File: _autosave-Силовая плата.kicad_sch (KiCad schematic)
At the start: 9 parts, among them Q1 BSP89, Q2 BSP89, Q3 BSP89, Q4 BSP89, Q5 BSP89, Q6 BSP89, U1 HIP2100_SOIC, U2 HIP2100_SOIC, U3 HIP2100_SOIC

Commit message: Вариант с транзисторами в линию
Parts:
- added J1, J2, J3: Conn_01x01, symbol Connector_Generic:Conn_01x01
- U1, U2, U3: footprint Package_DFN_QFN:DFN-8-1EP_3x3mm_P0.5mm_EP1.65x2.38mm -> Package_SO:SOIC-8_3.9x4.9mm_P1.27mm
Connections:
- net A: now also J1.1 (Pin_1)
- net B: now also J2.1 (Pin_1)
- net C: now also J3.1 (Pin_1)
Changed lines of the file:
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@@
+    )
+  )
+  (global_label "B" (shape input) (at 210.82 63.5 270) (fields_autoplaced)
+    (effects (font (size 1.27 1.27)) (justify right))
+    (property "Intersheetrefs" "${INTERSHEET_REFS}" (at 210.82 67.7552 90)
+      (effects (font (size 1.27 1.27)) (justify right) hide)
+    )
+  )
+  (global_label "C" (shape input) (at 220.98 63.5 270) (fields_autoplaced)
+    (effects (font (size 1.27 1.27)) (justify right))
+    (property "Intersheetrefs" "${INTERSHEET_REFS}" (at 220.98 67.7552 90)
+      (effects (font (size 1.27 1.27)) (justify right) hide)
     )
   )
@@
     )
   )
+  (global_label "A" (shape input) (at 200.66 63.5 270) (fields_autoplaced)
+    (effects (font (size 1.27 1.27)) (justify right))
+    (property "Intersheetrefs" "${INTERSHEET_REFS}" (at 200.66 67.5738 90)
+      (effects (font (size 1.27 1.27)) (justify right) hide)
+    )
+  )
   (global_label "G5" (shape input) (at 163.83 66.04 180) (fields_autoplaced)
     (effects (font (size 1.27 1.27)) (justify right))
@@
     )
   )
+  (symbol (lib_id "Connector_Generic:Conn_01x01") (at 220.98 58.42 90) (unit 1)
+    (in_bom yes) (on_board yes) (dnp no) (fields_autoplaced)
+    (property "Reference" "J3" (at 223.52 57.15 90)
+      (effects (font (size 1.27 1.27)) (justify right))
+    )
+    (property "Value" "Conn_01x01" (at 223.52 59.69 90)
+      (effects (font (size 1.27 1.27)) (justify right) hide)
+    )
+    (property "Footprint" "" (at 220.98 58.42 0)
+      (effects (font (size 1.27 1.27)) hide)
+    )
+    (property "Datasheet" "~" (at 220.98 58.42 0)
+      (effects (font (size 1.27 1.27)) hide)
+    )
+    (pin "1")
+    (instances
+      (project "Силовая плата"
+        (path "/96c6fc92-8ec6-44f7-b0dc-9ad8f1acea09"
+          (reference "J3") (unit 1)
+        )
+      )
+    )
+  )
   (symbol (lib_id "power:+12V") (at 130.81 58.42 0) (unit 1)
     (in_bom yes) (on_board yes) (dnp no) (fields_autoplaced)
@@
     )
   )
+  (symbol (lib_id "Connector_Generic:Conn_01x01") (at 210.82 58.42 90) (unit 1)
+    (in_bom yes) (on_board yes) (dnp no) (fields_autoplaced)
+    (property "Reference" "J2" (at 213.36 57.15 90)
+      (effects (font (size 1.27 1.27)) (justify right))
+    )
+    (property "Value" "Conn_01x01" (at 213.36 59.69 90)
+      (effects (font (size 1.27 1.27)) (justify right) hide)
+    )
+    (property "Footprint" "" (at 210.82 58.42 0)
+      (effects (font (size 1.27 1.27)) hide)
+    )
+    (property "Datasheet" "~" (at 210.82 58.42 0)
+      (effects (font (size 1.27 1.27)) hide)
+    )
+    (pin "1")
+    (instances
+      (project "Силовая плата"
+        (path "/96c6fc92-8ec6-44f7-b0dc-9ad8f1acea09"
+          (reference "J2") (unit 1)
+        )
+      )
+    )
+  )
+  (symbol (lib_id "Connector_Generic:Conn_01x01") (at 200.66 58.42 90) (unit 1)
+    (in_bom yes) (on_board yes) (dnp no) (fields_autoplaced)
+    (property "Reference" "J1" (at 203.2 57.15 90)
+      (effects (font (size 1.27 1.27)) (justify right))
+    )
+    (property "Value" "Conn_01x01" (at 203.2 59.69 90)
+      (effects (font (size 1.27 1.27)) (justify right) hide)
+    )
+    (property "Footprint" "" (at 200.66 58.42 0)
+      (effects (font (size 1.27 1.27)) hide)
+    )
+    (property "Datasheet" "~" (at 200.66 58.42 0)
+      (effects (font (size 1.27 1.27)) hide)
+    )
+    (pin "1")
+    (instances
+      (project "Силовая плата"
+        (path "/96c6fc92-8ec6-44f7-b0dc-9ad8f1acea09"
+          (reference "J1") (unit 1)
+        )
+      )
+    )
+  )
   (symbol (lib_id "Driver_FET:HIP2100_SOIC") (at 175.26 113.03 0) (unit 1)
     (in_bom yes) (on_board yes) (dnp no) (fields_autoplaced)
@@
       (effects (font (size 1.27 1.27)))
     )
-    (property "Footprint" "Package_DFN_QFN:DFN-8-1EP_3x3mm_P0.5mm_EP1.65x2.38mm" (at 175.26 125.73 0)
+    (property "Footprint" "Package_SO:SOIC-8_3.9x4.9mm_P1.27mm" (at 175.26 125.73 0)
       (effects (font (size 1.27 1.27) italic) hide)
     )
@@
       (effects (font (size 1.27 1.27)))
     )
-    (property "Footprint" "Package_DFN_QFN:DFN-8-1EP_3x3mm_P0.5mm_EP1.65x2.38mm" (at 154.94 125.73 0)
+    (property "Footprint" "Package_SO:SOIC-8_3.9x4.9mm_P1.27mm" (at 154.94 125.73 0)
       (effects (font (size 1.27 1.27) italic) hide)
     )
@@
       (effects (font (size 1.27 1.27)))
     )
-    (property "Footprint" "Package_DFN_QFN:DFN-8-1EP_3x3mm_P0.5mm_EP1.65x2.38mm" (at 104.14 86.36 0)
+    (property "Footprint" "Package_SO:SOIC-8_3.9x4.9mm_P1.27mm" (at 104.14 86.36 0)
       (effects (font (size 1.27 1.27) italic) hide)
     )

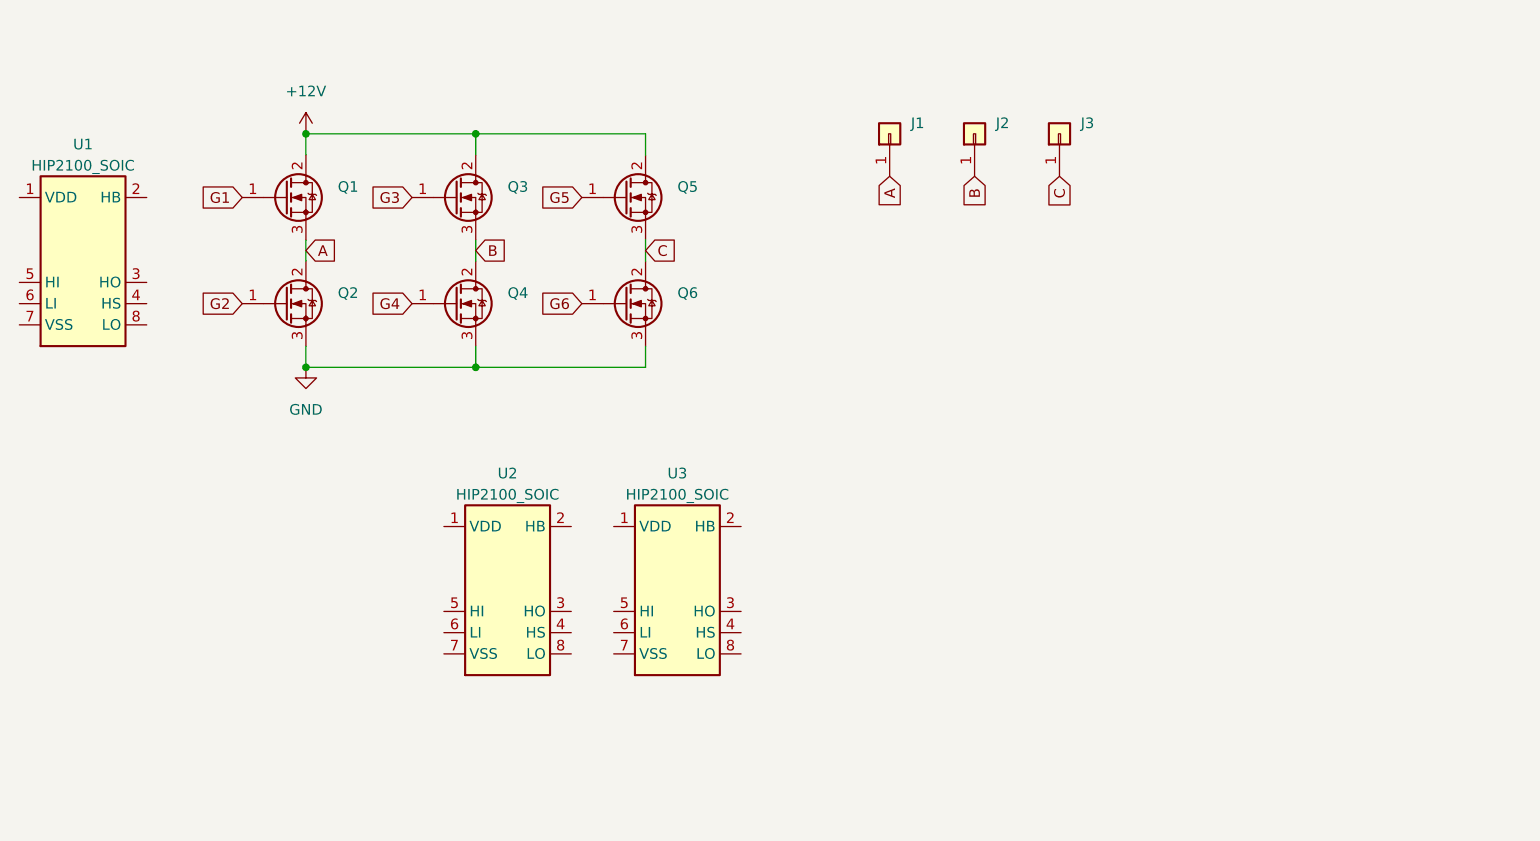
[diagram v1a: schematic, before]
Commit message: Добавил датчики тока и шунты
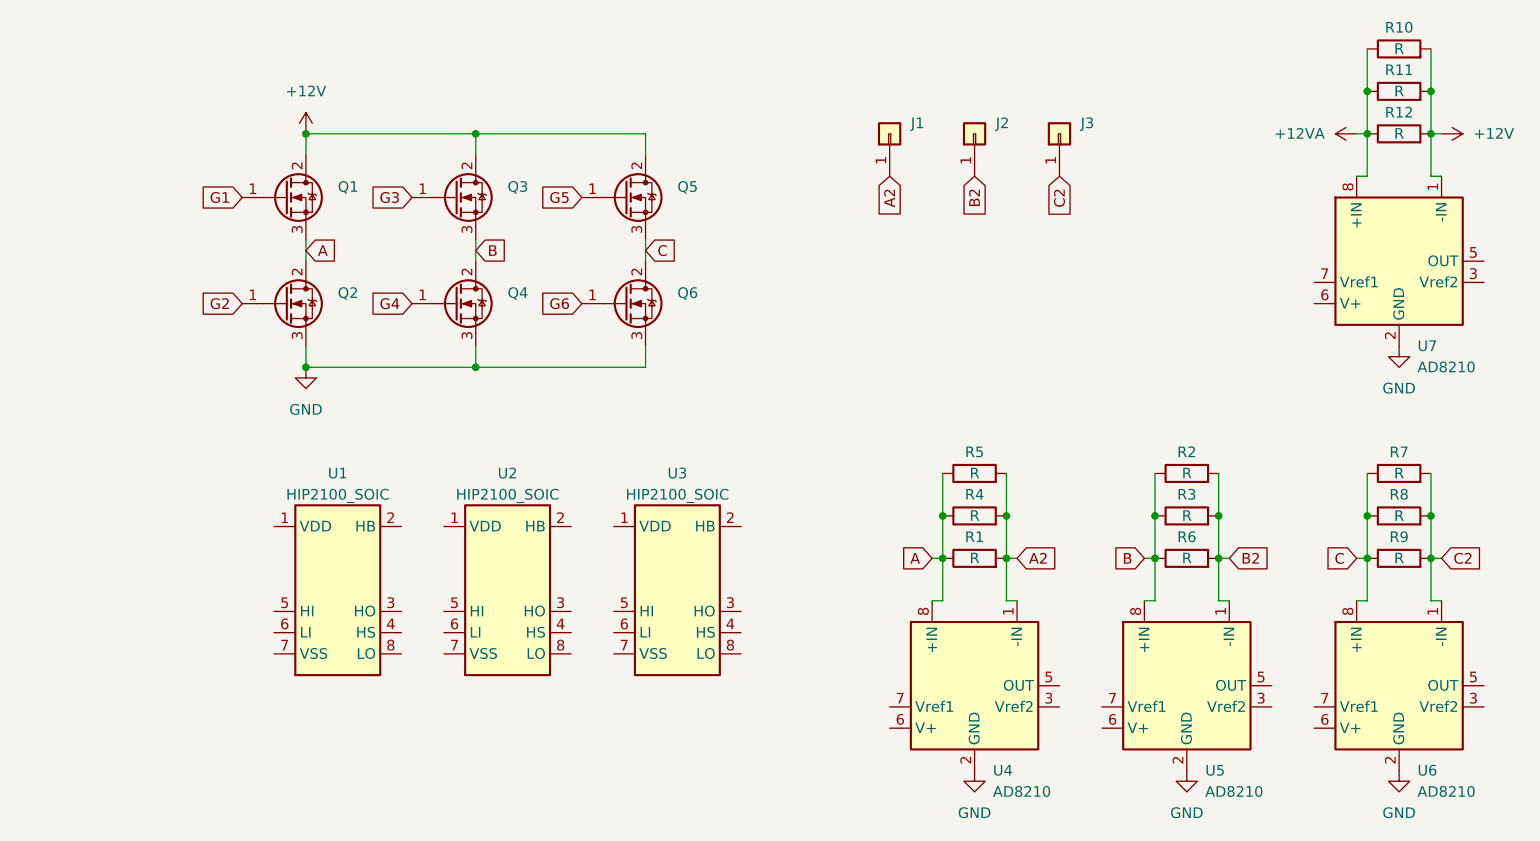
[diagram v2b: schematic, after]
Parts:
- added R1, R10, R11, R12, R2, R3, R4, R5, R6, R7, R8, R9: R, Resistor_SMD:R_2512_6332Metric_Pad1.40x3.35mm_HandSolder, symbol Device:R
- added U4, U5, U6, U7: AD8210, Package_SO:SOIC-8_3.9x4.9mm_P1.27mm, symbol Amplifier_Current:AD8210
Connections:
- net +12V: now also R10.2, R11.2, R12.2, U7.1 (-IN)
- net A: now also R1.1, R4.1, R5.1, U4.8 (+IN); no longer J1.1 (Pin_1)
- net B: now also R2.1, R3.1, R6.1, U5.8 (+IN); no longer J2.1 (Pin_1)
- net C: now also R7.1, R8.1, R9.1, U6.8 (+IN); no longer J3.1 (Pin_1)
- net GND: now also U4.2 (GND), U5.2 (GND), U6.2 (GND), U7.2 (GND)
- new net +12VA: R10.1, R11.1, R12.1, U7.8 (+IN)
- new net A2: J1.1 (Pin_1), R1.2, R4.2, R5.2, U4.1 (-IN)
- new net B2: J2.1 (Pin_1), R2.2, R3.2, R6.2, U5.1 (-IN)
- new net C2: J3.1 (Pin_1), R7.2, R8.2, R9.2, U6.1 (-IN)
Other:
- moved on the sheet: U1
